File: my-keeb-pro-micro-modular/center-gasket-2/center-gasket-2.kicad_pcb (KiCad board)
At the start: 2 copper layers, 95.2 x 100 mm, 50 parts, among them M1 1x5, M2 1x5, SW1 SW_Push, U1 ProMicro

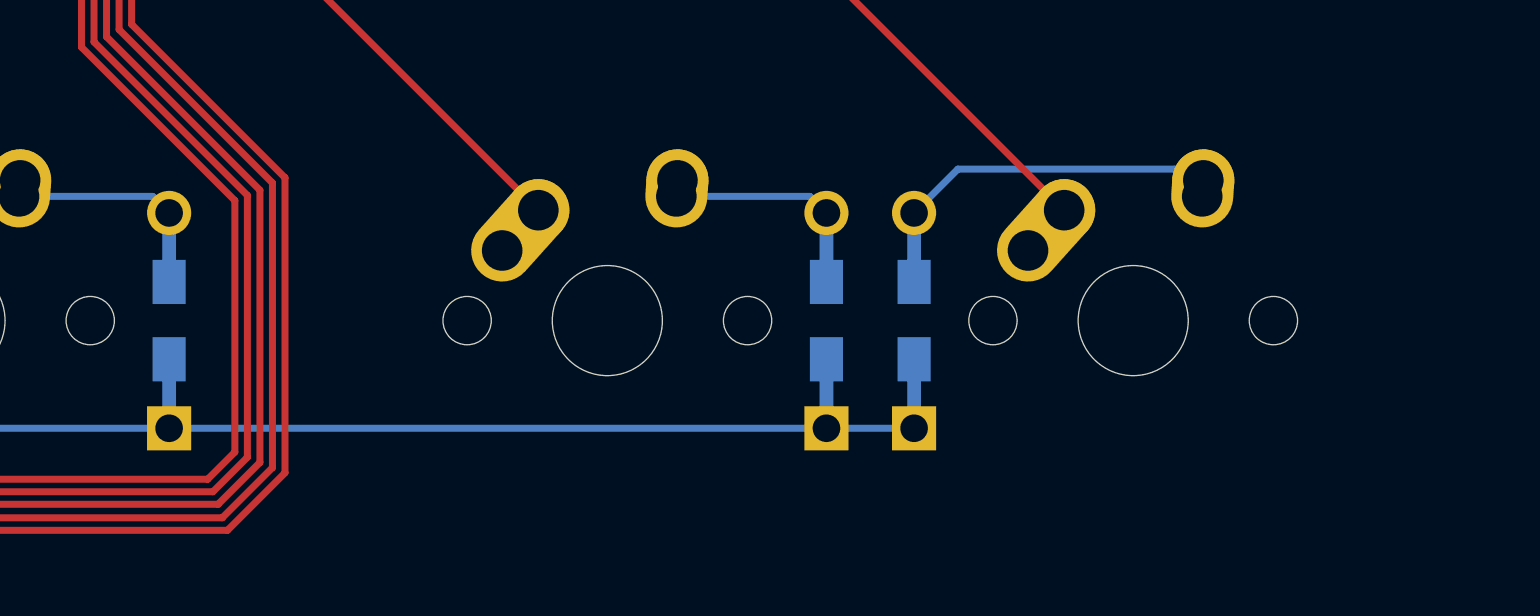
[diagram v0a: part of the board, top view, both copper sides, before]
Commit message: Added a gasket mount case file
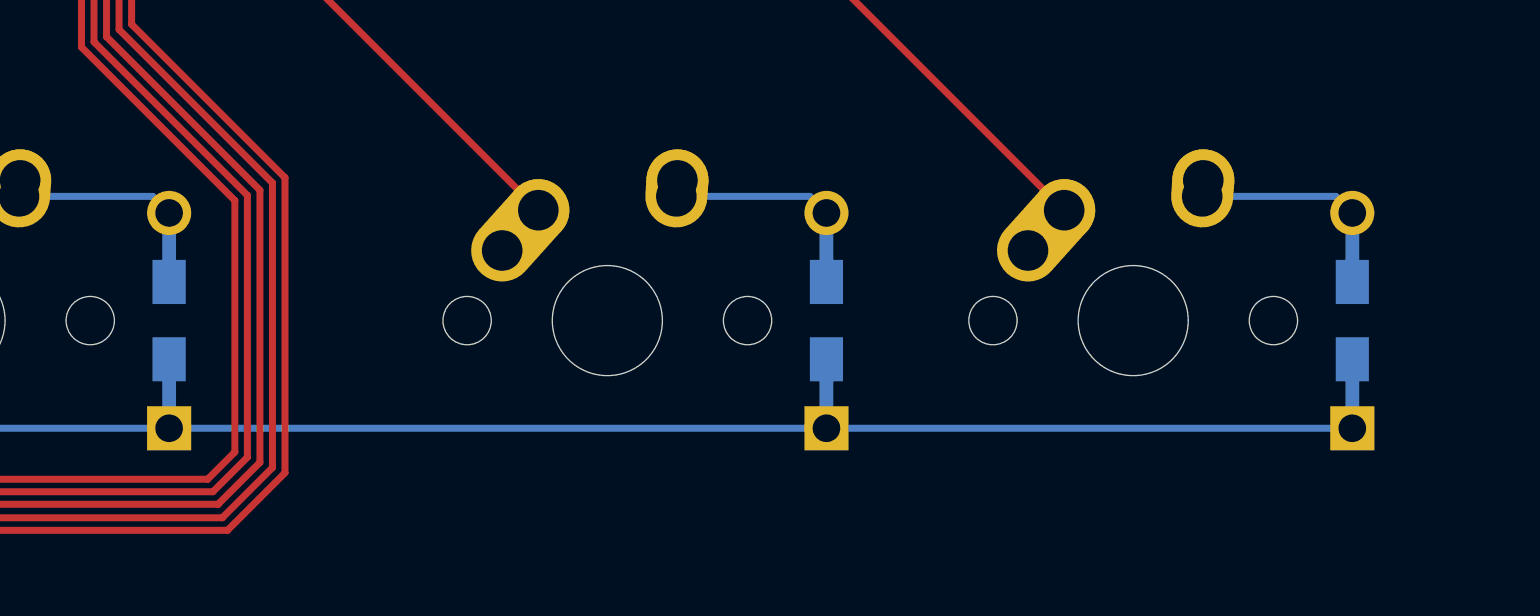
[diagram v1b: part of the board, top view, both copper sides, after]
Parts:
- D24, D25, D26, D27, D28, D29, D30, D31, D32, D33, D34, D35, D36, D37, D38, D39, D40, D41, D42, D43, D44, D45, D46: value SOD-123 -> D_Small
- moved D38 15.9 mm to (96.0, 116.7)
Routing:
- net ROW4: track 106.6 -> 122.5 mm
- net Net-(D38-Pad2): track 11.5 -> 5.69 mm
